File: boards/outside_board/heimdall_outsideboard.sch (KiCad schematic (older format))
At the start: 6 parts, among them J1 Conn_01x09, J2 Conn_01x06

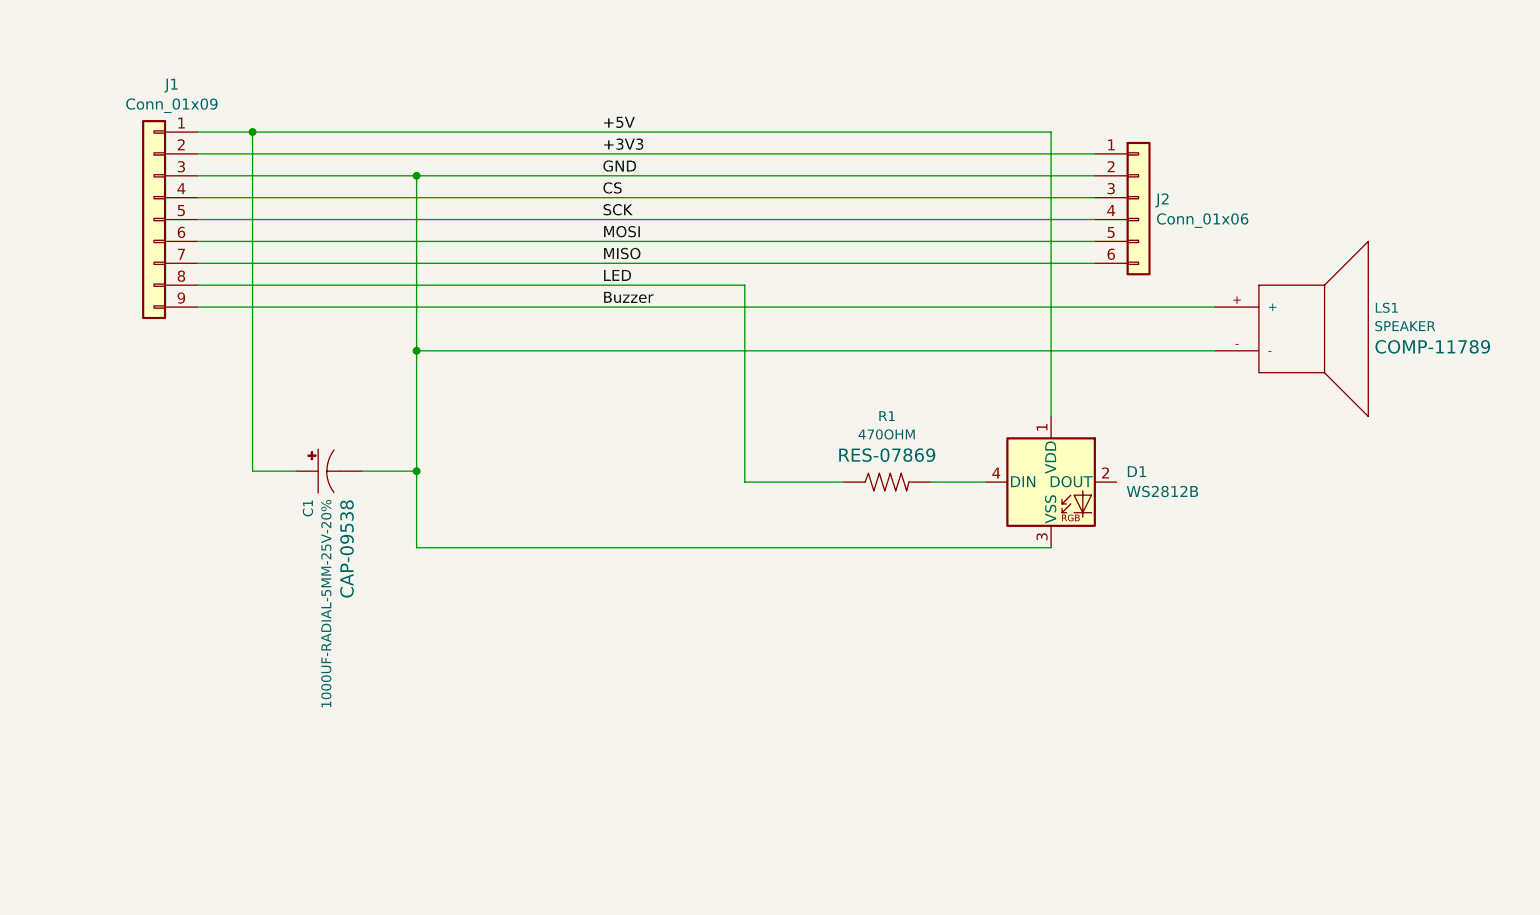
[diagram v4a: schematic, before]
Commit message: Update outside board schematics and board layout
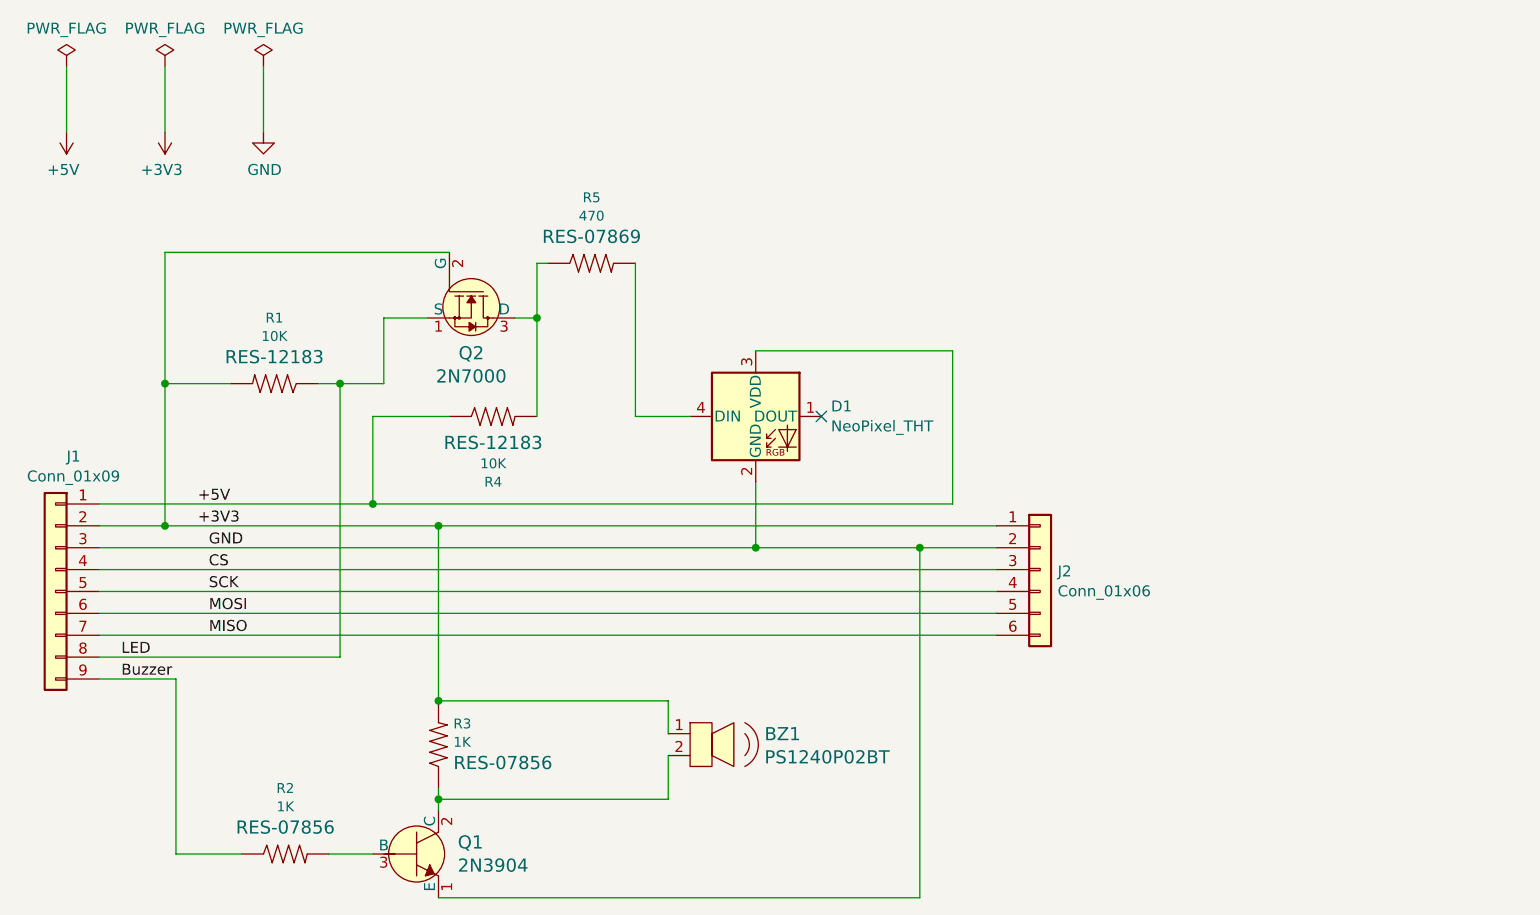
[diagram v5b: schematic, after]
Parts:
- removed C1: 1000UF-RADIAL-5MM-25V-20%, Capacitor_THT:CP_Radial_D12.5mm_P5.00mm, symbol SparkFun-Capacitors:1000UF-RADIAL-5MM-25V-20%
- removed D1: WS2812B, LED_SMD:LED_WS2812B_PLCC4_5.0x5.0mm_P3.2mm, symbol LED:WS2812B
- removed LS1: SPEAKER, Electromechanical:PCB_MOUNT_SPEAKER, symbol SparkFun-Electromechanical:SPEAKER
- removed R1: 470OHM, Resistor_THT:R_Axial_DIN0918_L18.0mm_D9.0mm_P22.86mm_Horizontal, symbol SparkFun-Resistors:470OHM
- added BZ1: PS1240P02BT, digikey-footprints:Piezo_Transducer_THT_PS1240P02BT, symbol dk_Alarms-Buzzers-and-Sirens:PS1240P02BT
- added D1: NeoPixel_THT, LED:WS2812B, symbol LED:NeoPixel_THT
- added Q1: 2N3904, Package_TO_SOT_THT:TO-92_Inline, symbol dk_Transistors-Bipolar-BJT-Single:2N3904
- added Q2: 2N7000, Package_TO_SOT_THT:TO-92_Inline, symbol dk_Transistors-FETs-MOSFETs-Single:2N7000
- added R1, R4: 10K, Resistor_THT:R_Axial_DIN0207_L6.3mm_D2.5mm_P10.16mm_Horizontal, symbol SparkFun-Resistors:10KOHM-HORIZ-1_4W-1%
- added R2, R3: 1K, Resistor_THT:R_Axial_DIN0207_L6.3mm_D2.5mm_P10.16mm_Horizontal, symbol SparkFun-Resistors:1KOHM-0603-1_10W-1%
- added R5: 470, Resistor_THT:R_Axial_DIN0207_L6.3mm_D2.5mm_P10.16mm_Horizontal, symbol SparkFun-Resistors:470OHM-0603-1_10W-1%
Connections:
- net +3V3: now also BZ1.1, Q2.2 (G), R1.2, R3.2
- net +5V: now also D1.3 (VDD), R4.1
- net Buzzer: now also R2.1
- net GND: now also D1.2 (GND), Q1.1 (E)
- net LED: now also Q2.1 (S), R1.1
- new net: D1.4 (DIN), R5.2
- new net: BZ1.2, Q1.2 (C), R3.1
- new net: Q2.3 (D), R4.2, R5.1
- new net: Q1.3 (B), R2.2
- no-connect marks 0 -> 1
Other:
- moved on the sheet: J1, J2

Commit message: Update outside board schematics and layout to revision 2
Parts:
- removed Q1: 2N3904, Package_TO_SOT_THT:TO-92_Inline, symbol dk_Transistors-Bipolar-BJT-Single:2N3904
- added J3, J4, J5, J6: Conn_01x01_Male, Connector_PinHeader_2.54mm:PinHeader_1x01_P2.54mm_Vertical, symbol Connector:Conn_01x01_Male
- added Q1: 2N3904, Package_TO_SOT_THT:TO-92_Inline, symbol Transistor_BJT:2N3904
- D1: footprint LED:WS2812B -> LED_THT:LED_D5.0mm-4_RGB
- R5: value 470 -> 500
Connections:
- net +3V3: now also J3.1 (Pin_1)
- net +5V: now also J6.1 (Pin_1)
- net GND: now also Q1.1 (E)
- net at D1.4 (DIN), R5.2: now also J5.1 (Pin_1)
- net at BZ1.2, R3.1: now also J4.1 (Pin_1), Q1.3 (C)
- net at R2.2: now also Q1.2 (B)
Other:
- moved on the sheet: D1
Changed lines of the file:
@@
 Sheet 1 1
 Title "Heimdall Outside Board"
-Date "2020-07-24"
-Rev "01"
+Date "2020-11-07"
+Rev "02"
 Comp ""
 Comment1 "https://opensource.org/licenses/MIT"
@@
 L LED:NeoPixel_THT D1
 U 1 1 5F17E8A3
-P 4350 4950
-F 0 "D1" H 4694 4996 50  0000 L CNN
-F 1 "NeoPixel_THT" H 4694 4905 50  0000 L CNN
-F 2 "LED:WS2812B" H 4400 4650 50  0001 L TNN
-F 3 "https://www.adafruit.com/product/1938" H 4450 4575 50  0001 L TNN
-	1    4350 4950
+P 4550 4950
+F 0 "D1" H 4894 4996 50  0000 L CNN
+F 1 "NeoPixel_THT" H 4894 4905 50  0000 L CNN
+F 2 "LED_THT:LED_D5.0mm-4_RGB" H 4600 4650 50  0001 L TNN
+F 3 "https://www.adafruit.com/product/1938" H 4650 4575 50  0001 L TNN
+	1    4550 4950
 	1    0    0    -1
 $EndComp
@@
 	1700 6950 2000 6950
 Wire Wire Line
-	2900 6750 2900 6700
-Wire Wire Line
 	2900 6250 2900 5450
-Wire Wire Line
-	2900 6250 3950 6250
-Wire Wire Line
-	3950 6250 3950 6400
-Connection ~ 2900 6250
-Wire Wire Line
-	3950 6500 3950 6700
-Wire Wire Line
-	3950 6700 2900 6700
-Connection ~ 2900 6700
-Wire Wire Line
-	2900 6700 2900 6650
 Wire Wire Line
 	5100 7150 5100 5550
@@
 Connection ~ 3350 4500
 Wire Wire Line
-	3800 4250 3800 4950
-Wire Wire Line
-	3800 4950 4050 4950
-Wire Wire Line
 	2850 4500 2650 4500
-$Comp
-L SparkFun-Resistors:470OHM-0603-1_10W-1% R5
-U 1 1 5F209E6B
-P 3600 4250
-F 0 "R5" H 3600 4550 45  0000 C CNN
-F 1 "470" H 3600 4466 45  0000 C CNN
-F 2 "Resistor_THT:R_Axial_DIN0207_L6.3mm_D2.5mm_P10.16mm_Horizontal" H 3600 4400 20  0001 C CNN
-F 3 "" H 3600 4250 60  0001 C CNN
-F 4 "RES-07869" H 3600 4371 60  0000 C CNN "Field4"
-	1    3600 4250
-	1    0    0    -1
-$EndComp
 Wire Wire Line
 	1350 5450 1650 5450
@@
 Wire Wire Line
 	5250 5350 5250 4650
-Wire Wire Line
-	5250 4650 4350 4650
-Wire Wire Line
-	1350 5550 4350 5550
-Wire Wire Line
-	4350 5550 4350 5250
-Connection ~ 4350 5550
-Wire Wire Line
-	4350 5550 5100 5550
 $Comp
 L power:PWR_FLAG #FLG01
@@
 F 3 "~" H 2100 3350 50  0001 C CNN
 	1    2100 3350
-	1    0    0    -1
-$EndComp
-$Comp
-L dk_Transistors-Bipolar-BJT-Single:2N3904 Q1
-U 1 1 5F2401CC
-P 2800 6950
-F 0 "Q1" H 2988 7003 60  0000 L CNN
-F 1 "2N3904" H 2988 6897 60  0000 L CNN
-F 2 "Package_TO_SOT_THT:TO-92_Inline" H 3000 7150 60  0001 L CNN
-F 3 "https://my.centralsemi.com/get_document.php?cmp=1&mergetype=pd&mergepath=pd&pdf_id=LSSGP072.PDF" H 3000 7250 60  0001 L CNN
-F 4 "2N3904CS-ND" H 3000 7350 60  0001 L CNN "Digi-Key_PN"
-F 5 "2N3904" H 3000 7450 60  0001 L CNN "MPN"
-F 6 "Discrete Semiconductor Products" H 3000 7550 60  0001 L CNN "Category"
-F 7 "Transistors - Bipolar (BJT) - Single" H 3000 7650 60  0001 L CNN "Family"
-F 8 "https://my.centralsemi.com/get_document.php?cmp=1&mergetype=pd&mergepath=pd&pdf_id=LSSGP072.PDF" H 3000 7750 60  0001 L CNN "DK_Datasheet_Link"
-F 9 "/product-detail/en/central-semiconductor-corp/2N3904/2N3904CS-ND/4806876" H 3000 7850 60  0001 L CNN "DK_Detail_Page"
-F 10 "TRANS NPN 40V TO-92" H 3000 7950 60  0001 L CNN "Description"
-F 11 "Central Semiconductor Corp" H 3000 8050 60  0001 L CNN "Manufacturer"
-F 12 "Active" H 3000 8150 60  0001 L CNN "Status"
-	1    2800 6950
 	1    0    0    -1
 $EndComp
@@
 Wire Wire Line
 	2100 3350 2100 3650
+$Comp
+L Connector:Conn_01x01_Male J3
+U 1 1 5FA614DC
+P 3350 6250
+F 0 "J3" H 3458 6431 50  0000 C CNN
+F 1 "Conn_01x01_Male" H 3458 6340 50  0000 C CNN
+F 2 "Connector_PinHeader_2.54mm:PinHeader_1x01_P2.54mm_Vertical" H 3350 6250 50  0001 C CNN
+F 3 "~" H 3350 6250 50  0001 C CNN
+	1    3350 6250
+	1    0    0    -1
+$EndComp
+$Comp
+L Connector:Conn_01x01_Male J4
+U 1 1 5FA62088
+P 3400 6800
+F 0 "J4" H 3508 6981 50  0000 C CNN
+F 1 "Conn_01x01_Male" H 3508 6890 50  0000 C CNN
+F 2 "Connector_PinHeader_2.54mm:PinHeader_1x01_P2.54mm_Vertical" H 3400 6800 50  0001 C CNN
+F 3 "~" H 3400 6800 50  0001 C CNN
+	1    3400 6800
+	1    0    0    -1
+$EndComp
+$Comp
+L Connector:Conn_01x01_Male J5
+U 1 1 5FA690EE
+P 3850 4950
+F 0 "J5" H 3958 5131 50  0000 C CNN
+F 1 "Conn_01x01_Male" H 3958 5040 50  0000 C CNN
+F 2 "Connector_PinHeader_2.54mm:PinHeader_1x01_P2.54mm_Vertical" H 3850 4950 50  0001 C CNN
+F 3 "~" H 3850 4950 50  0001 C CNN
+	1    3850 4950
+	1    0    0    -1
+$EndComp
+$Comp
+L Connector:Conn_01x01_Male J6
+U 1 1 5FA69F83
+P 4650 4650
+F 0 "J6" H 4758 4831 50  0000 C CNN
+F 1 "Conn_01x01_Male" H 4758 4740 50  0000 C CNN
+F 2 "Connector_PinHeader_2.54mm:PinHeader_1x01_P2.54mm_Vertical" H 4650 4650 50  0001 C CNN
+F 3 "~" H 4650 4650 50  0001 C CNN
+	1    4650 4650
+	1    0    0    -1
+$EndComp
+Wire Wire Line
+	1350 5550 4550 5550
+Wire Wire Line
+	4550 5250 4550 5550
+Connection ~ 4550 5550
+Wire Wire Line
+	4550 5550 5100 5550
+Wire Wire Line
+	3850 4250 3800 4250
+Wire Wire Line
+	4050 4950 4250 4950
+Wire Wire Line
+	4850 4650 5250 4650
+Wire Wire Line
+	2900 6650 2900 6750
+Wire Wire Line
+	3950 6400 3950 6250
+Wire Wire Line
+	3950 6250 3550 6250
+Wire Wire Line
+	3550 6250 2900 6250
+Connection ~ 3550 6250
+Connection ~ 2900 6250
+Wire Wire Line
+	3950 6500 3950 6800
+Wire Wire Line
+	3950 6800 3600 6800
+Wire Wire Line
+	3600 6800 3050 6800
+Wire Wire Line
+	3050 6800 3050 6650
+Wire Wire Line
+	3050 6650 2900 6650
+Connection ~ 3600 6800
+Connection ~ 2900 6650
+Wire Wire Line
+	4850 4650 4550 4650
+Connection ~ 4850 4650
+Wire Wire Line
+	4050 4950 3850 4950
+Wire Wire Line
+	3850 4950 3850 4250
+Connection ~ 4050 4950
+$Comp
+L Transistor_BJT:2N3904 Q1
+U 1 1 5FA8FEA8
+P 2800 6950
+F 0 "Q1" H 2990 6996 50  0000 L CNN
+F 1 "2N3904" H 2990 6905 50  0000 L CNN
+F 2 "Package_TO_SOT_THT:TO-92_Inline" H 3000 6875 50  0001 L CIN
+F 3 "https://www.onsemi.com/pub/Collateral/2N3903-D.PDF" H 2800 6950 50  0001 L CNN
+	1    2800 6950
+	1    0    0    -1
+$EndComp
+$Comp
+L SparkFun-Resistors:470OHM-0603-1_10W-1% R5
+U 1 1 5F209E6B
+P 3600 4250
+F 0 "R5" H 3600 4550 45  0000 C CNN
+F 1 "500" H 3600 4466 45  0000 C CNN
+F 2 "Resistor_THT:R_Axial_DIN0207_L6.3mm_D2.5mm_P10.16mm_Horizontal" H 3600 4400 20  0001 C CNN
+F 3 "" H 3600 4250 60  0001 C CNN
+F 4 "RES-07869" H 3600 4371 60  0000 C CNN "Field4"
+	1    3600 4250
+	1    0    0    -1
+$EndComp
 $EndSCHEMATC
